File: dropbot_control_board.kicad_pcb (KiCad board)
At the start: 2 copper layers, 83.8 x 56.1 mm, 49 parts, among them J2 COMM_BUS, P3 POWER, P4 VOUT, P5 LIGHT, P6 MAGNET, P7 CONN_01X05, P8 CONN_01X03, Q1 IRF644PBF, Q2 TIP120, Q3 2N7002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

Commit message: Rename dropbot-control-board
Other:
- board text added: "DropBot control board v0.1"
- board text removed: "HV signal generator board v0.3"
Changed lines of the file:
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@@
   (page USLetter)
   (title_block
-    (title "HV signal generator board")
-    (date 2016-04-16)
-    (rev 0.3)
-    (company "Ryan Fobel")
+    (title "DropBot control board")
+    (date 2016-09-20)
+    (rev 0.1)
+    (company Sci-bots)
   )
   (layers
@@
     )
   )
-  (gr_text "HV signal generator board v0.3" (at 18.161 70.231) (layer F.SilkS)
+  (gr_text "DropBot control board v0.1" (at 18.161 70.231) (layer F.SilkS)
     (effects (font (size 1 1) (thickness 0.2)) (justify left))
   )

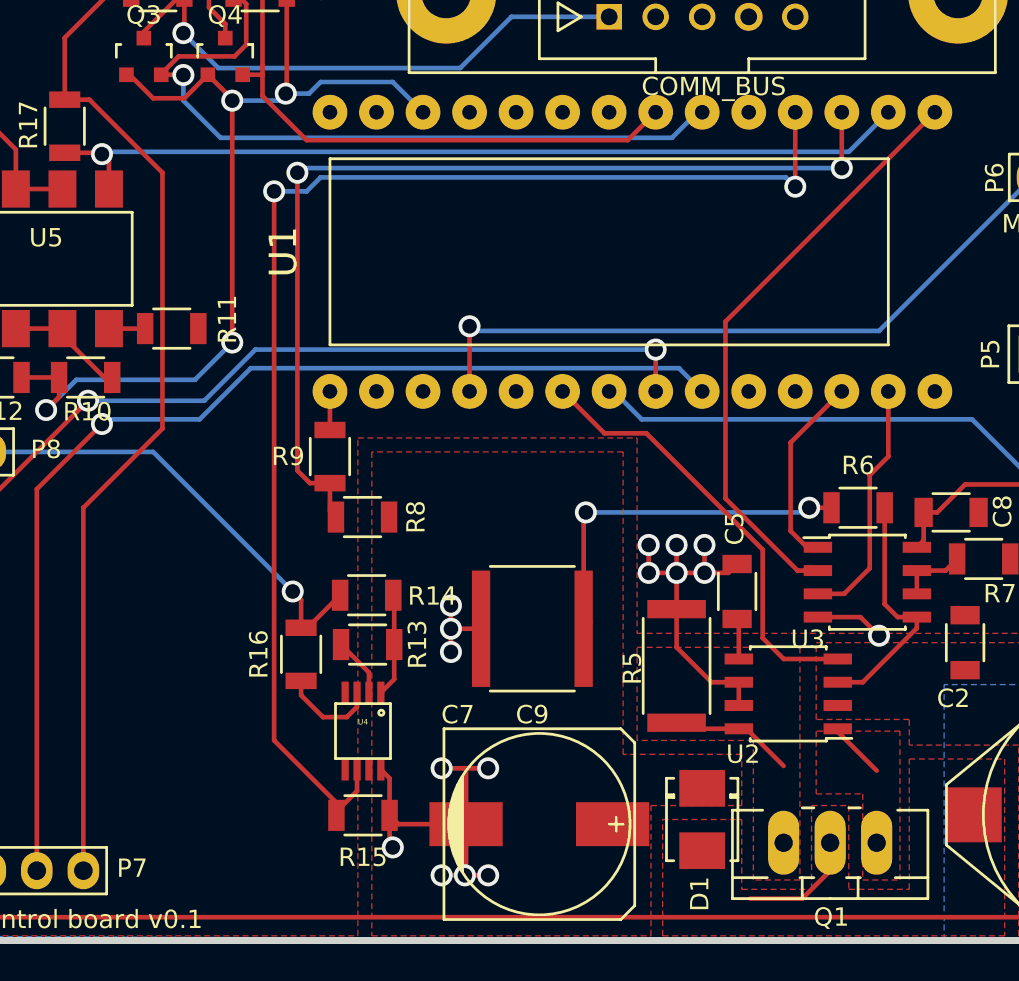
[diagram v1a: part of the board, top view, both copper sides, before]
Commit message: Fix routing of D3/OUTPUT_SELECT and add MAX1771...
Fix routing of D3/OUTPUT_SELECT and add MAX1771 current sensing.
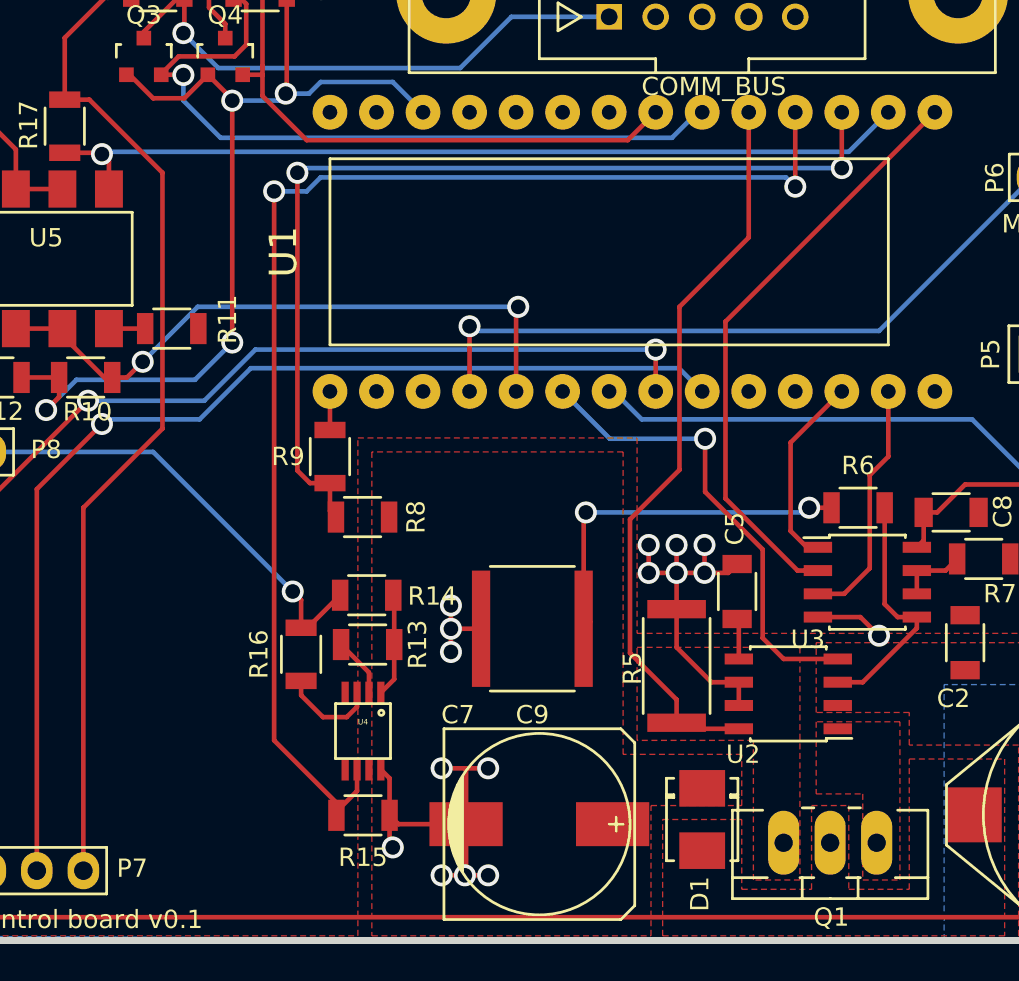
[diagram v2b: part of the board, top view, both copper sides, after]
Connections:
- net A2/CURRENT_SENSE renamed A2/HV507_CS
- Q1 pad 3: Net-(Q1-Pad3) -> A3/MAX1771_CS
- R10 pad 2: A3/OUTPUT_SELECT -> D3/OUTPUT_SELECT
- R5 pad 1: Net-(Q1-Pad3) -> A3/MAX1771_CS
- U1 pad 17: Net-(U1-Pad17) -> A3/MAX1771_CS
- U1 pad 3: Net-(U1-Pad3) -> D3/OUTPUT_SELECT
- U2 pad 8: Net-(Q1-Pad3) -> A3/MAX1771_CS
- U5 pad 2: A3/OUTPUT_SELECT -> D3/OUTPUT_SELECT
- U5 pad 3: A3/OUTPUT_SELECT -> D3/OUTPUT_SELECT
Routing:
- net A3/MAX1771_CS: track 0.00 -> 41.2 mm
- net D3/OUTPUT_SELECT: track 0.00 -> 35.4 mm, vias 0 -> 2
- net A3/OUTPUT_SELECT: track 7.02 -> 0.00 mm
- net Net-(Q1-Pad3): track 7.00 -> 0.00 mm
- net Net-(D1-Pad2): track 8.49 -> 3.49 mm
- net Net-(Q1-Pad1): track 3.51 -> 0.70 mm
- net D4/SHDN: track 23.9 -> 25.6 mm, vias 0 -> 1
- added copper zone on F.Cu, net A3/MAX1771_CS
- removed copper zone on F.Cu, net Net-(Q1-Pad3)

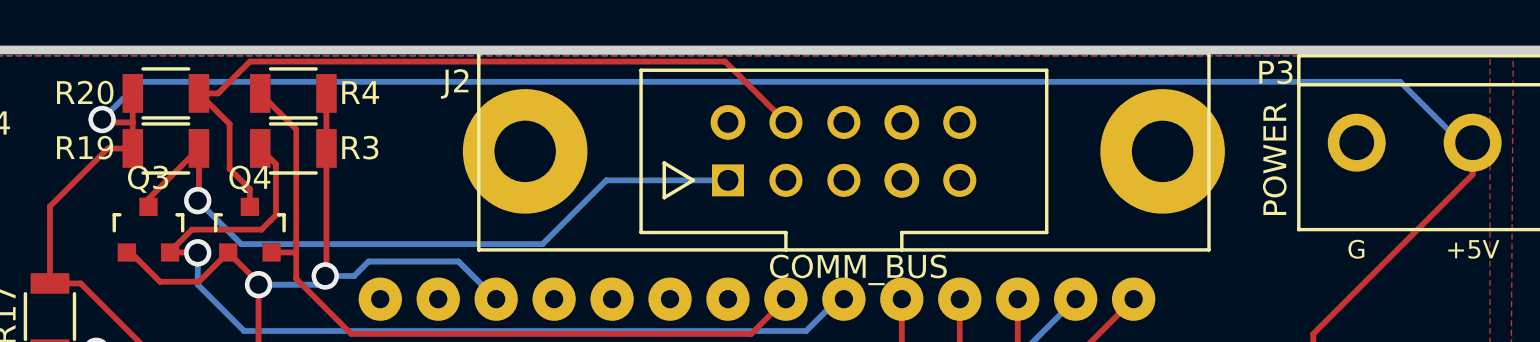
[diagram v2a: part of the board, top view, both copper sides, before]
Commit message: Connect 5V pin on COMM_BUS
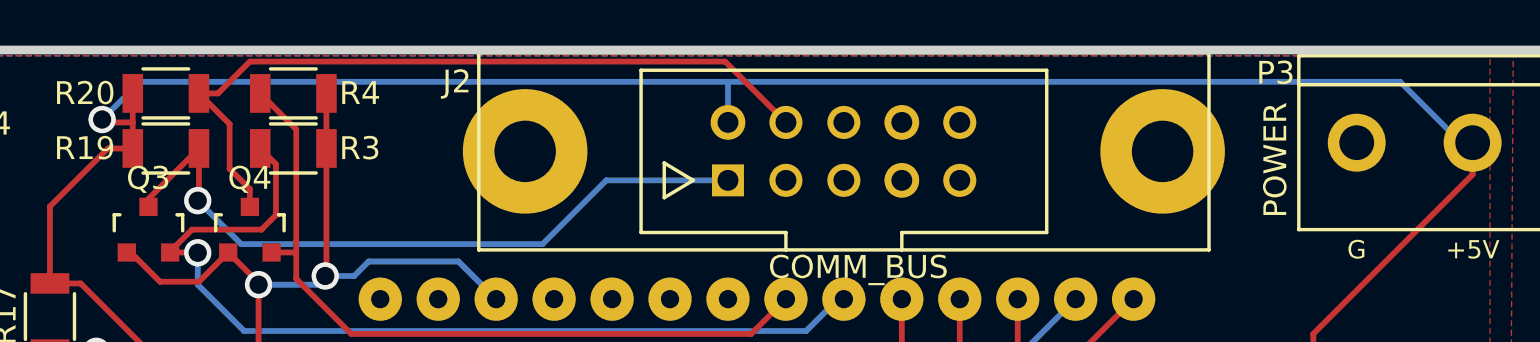
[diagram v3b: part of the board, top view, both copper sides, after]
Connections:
- J2 pad 2: Net-(J2-Pad2) -> +5V
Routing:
- net +5V: track 171.6 -> 173.4 mm

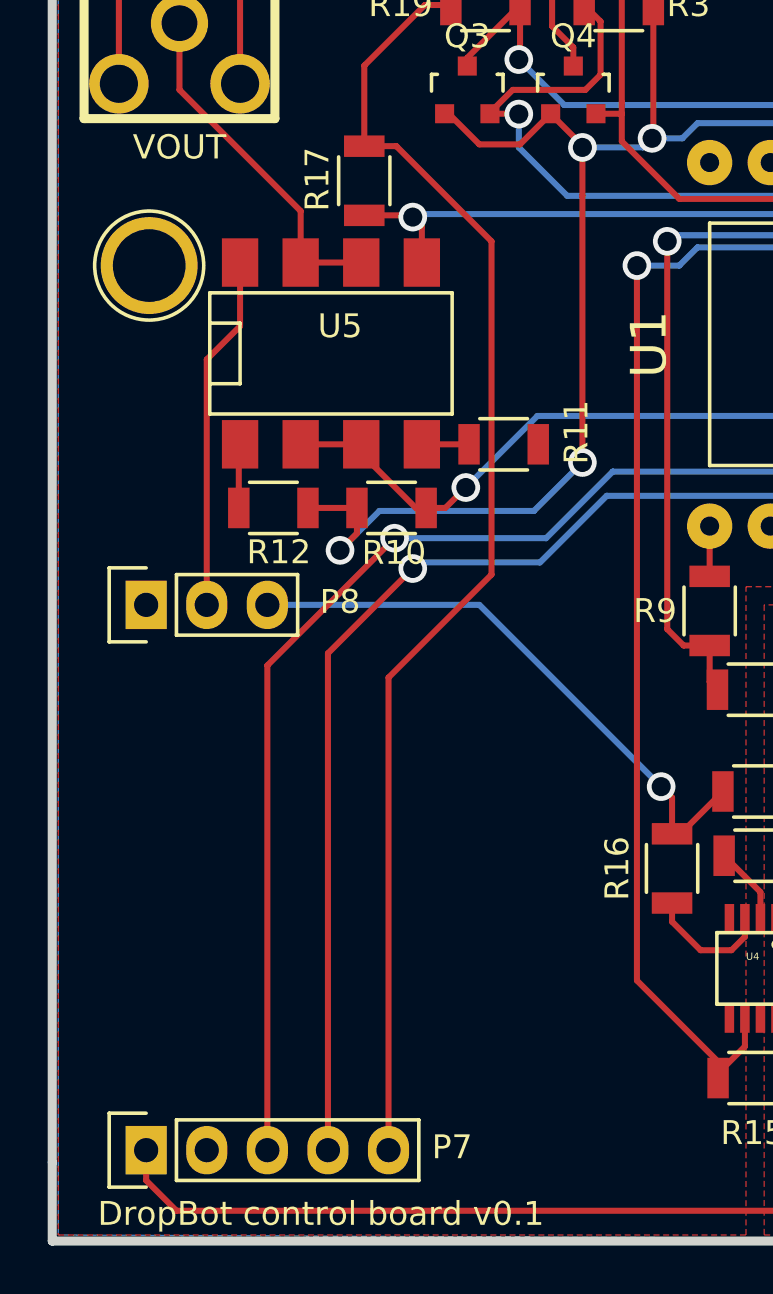
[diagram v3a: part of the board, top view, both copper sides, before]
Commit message: [WIP] Integrate HV square-wave driver (not routed)
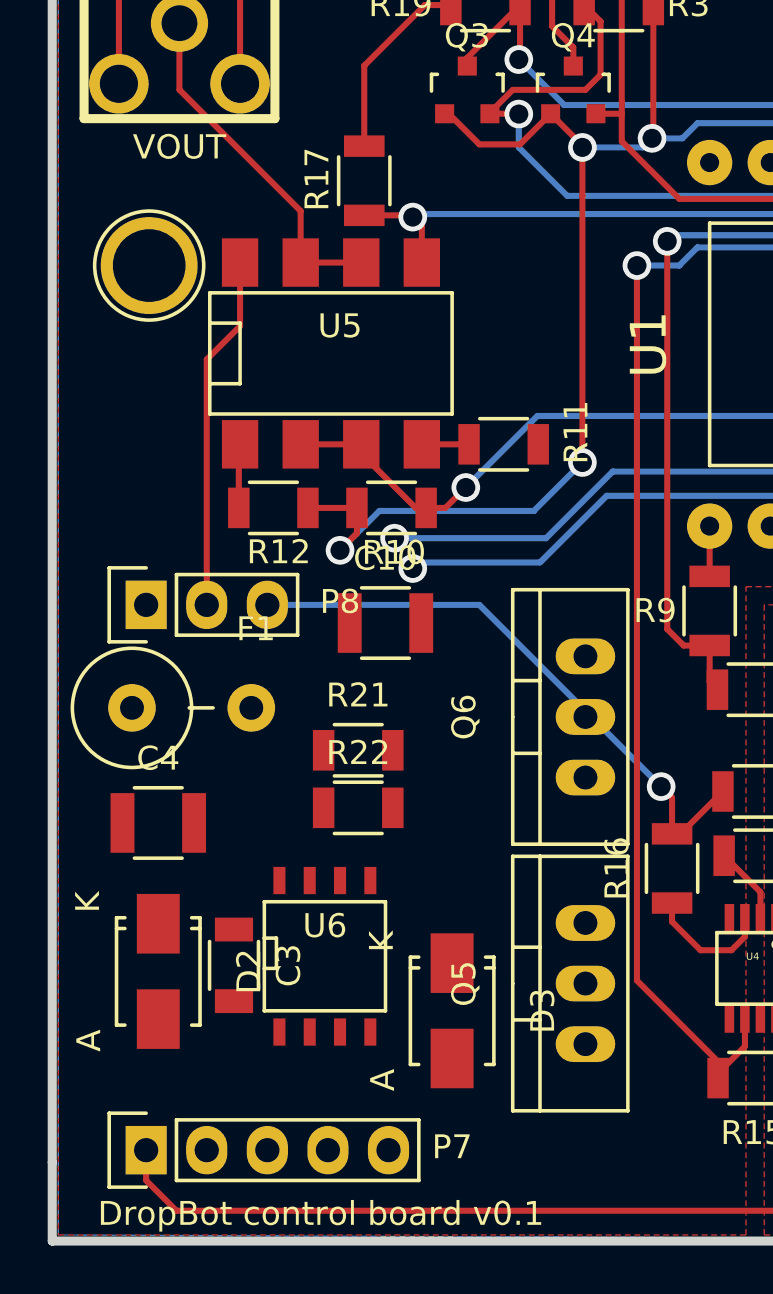
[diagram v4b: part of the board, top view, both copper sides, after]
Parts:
- added C10: C, Capacitors_SMD:C_1210, F.Cu at (30.2, 45.5)
- added C3: 0.1uF, Capacitors_SMD:C_1206, F.Cu at (23.9, 59.8)
- added C4: 0.1uF, Capacitors_SMD:C_1210, F.Cu at (20.7, 53.8)
- added D2: D, Diodes_SMD:SMA_Standard, F.Cu at (20.7, 60.1)
- added D3: D, Diodes_SMD:SMA_Standard, F.Cu at (33.0, 61.7)
- added F1: FUSE, Resistors_ThroughHole:Resistor_Vertical_RM5mm, F.Cu at (22.1, 49.0)
- added Q5: Q_NMOS_GDS, TO_SOT_Packages_THT:TO-220_Neutral123_Vertical, F.Cu at (38.6, 60.6)
- added Q6: Q_NMOS_GDS, TO_SOT_Packages_THT:TO-220_Neutral123_Vertical, F.Cu at (38.6, 49.4)
- added R21: 10, Resistors_SMD:R_1206, F.Cu at (29.1, 50.8)
- added R22: R, Resistors_SMD:R_1206, F.Cu at (29.1, 53.2)
- added U6: NCP5304, SMD_Packages:SOIC-8-N, F.Cu at (27.7, 59.4)
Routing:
- net +5V: track 173.4 -> 126.5 mm
- net D6/DRIVER_HI: track 62.3 -> 34.4 mm
- net D7/DRIVER_LO: track 60.7 -> 34.8 mm

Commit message: Re-do layout
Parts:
- added C11: 1uF, Capacitors_SMD:C_0805, F.Cu at (57.3, 45.0)
- added C12: 1pF, Capacitors_SMD:C_0805, F.Cu at (34.0, 50.0)
- added C13: 10pF, Capacitors_SMD:C_0805, F.Cu at (38.9, 49.9)
- added C14: 100pF, Capacitors_SMD:C_0805, F.Cu at (44.2, 49.9)
- added C15: 1nF, Capacitors_SMD:C_0805, F.Cu at (48.0, 49.9)
- added C16: 0.1uF, Capacitors_SMD:C_0805, F.Cu at (71.6, 44.1)
- added C17: 0.1uF, Capacitors_SMD:C_0805, F.Cu at (71.8, 38.0)
- added C18: 0.1uF, Capacitors_SMD:C_0805, F.Cu at (75.3, 38.2)
- added C19: 4.7nF, Capacitors_SMD:C_0805, F.Cu at (63.1, 46.7)
- added C20: 1nF, Capacitors_SMD:C_0805, F.Cu at (62.5, 35.2)
- added C21: 0.15uF, Capacitors_SMD:C_0805, F.Cu at (60.8, 37.5)
- added C22: 1nF, Capacitors_SMD:C_0805, F.Cu at (65.8, 47.6)
- added G***: LOGO, LOGO, F.Cu at (49.4, 89.2)
- added G***: LOGO, LOGO, F.Cu at (50.9, 83.2)
- added G***: LOGO, LOGO, F.Cu at (96.6, 50.4)
- added IC1: MCP6024, SMD_Packages:SOIC-14_N, F.Cu at (66.5, 40.5)
- added P1: FEEDBACK, footprints:JACK_SMA, F.Cu at (40.5, 28.2)
- added R23: 1Meg, Resistors_SMD:R_0805, F.Cu at (55.9, 42.4)
- added R24: 200, Resistors_SMD:R_0805, F.Cu at (33.8, 37.6)
- added R25: 10k, Resistors_SMD:R_0805, F.Cu at (72.8, 40.9)
- added R26: 2.2k, Resistors_SMD:R_0805, F.Cu at (73.5, 38.2)
- added R27: 1Meg, Resistors_SMD:R_0805, F.Cu at (73.5, 43.9)
- added R28: 200, Resistors_SMD:R_0805, F.Cu at (39.6, 37.6)
- added R29: 200, Resistors_SMD:R_0805, F.Cu at (45.0, 37.6)
- added R30: 200, Resistors_SMD:R_0805, F.Cu at (49.8, 37.6)
- added R31: 1.91k, Resistors_SMD:R_0805, F.Cu at (60.8, 39.2)
- added R32: 16.9k, Resistors_SMD:R_0805, F.Cu at (61.3, 44.7)
- added R33: 806, Resistors_SMD:R_0805, F.Cu at (60.8, 42.0)
- added R34: 13.3k, Resistors_SMD:R_0805, F.Cu at (60.3, 47.1)
- added U7: AQW216, SMD_Packages:DIP-8_SMD, F.Cu at (37.2, 43.7)
- added U8: AQW216, SMD_Packages:DIP-8_SMD, F.Cu at (47.9, 43.7)
- C2, C3, C5, C8: footprint Capacitors_SMD:C_1206 -> Capacitors_SMD:C_0805
- P7: value CONN_01X05 -> CONN_01X04; footprint Pin_Headers:Pin_Header_Straight_1x05 -> Pin_Headers:Pin_Header_Straight_1x04
- Q1, Q2: footprint TO_SOT_Packages_THT:TO-220_Neutral123_Vertical_LargePads -> TO_SOT_Packages_THT:TO-220_Neutral123_Horizontal_LargePads; moved to B.Cu
- Q5, Q6: footprint TO_SOT_Packages_THT:TO-220_Neutral123_Vertical -> TO_SOT_Packages_THT:TO-220_Neutral123_Horizontal_LargePads; moved to B.Cu
- R1, R10, R11, R12, R13, R14, R15, R16, R17, R18, R19, R2, R20, R21, R22, R3, R4, R7, R9: footprint Resistors_SMD:R_1206 -> Resistors_SMD:R_0805
- U1: value Teensy_3.1 -> Teensy_3.2; footprint footprints:Teensy-3.1 -> footprints:Teensy-3.2
- moved Q3 53.2 mm to (81.5, 46.2)
- moved R19 53.2 mm to (82.3, 42.7)
- moved R20 53.2 mm to (82.3, 40.3)
- moved Q4 53.2 mm to (86.0, 46.2)
- moved R3 53.2 mm to (87.9, 42.7)
- moved R4 53.2 mm to (87.9, 40.3)
- moved R14 35.1 mm to (69.6, 78.4)
- moved C3 33.6 mm to (39.8, 89.4), turned to 180 degrees
- moved R6 32.0 mm to (73.7, 79.8), turned to 90 degrees
- moved R9 31.6 mm to (61.6, 71.1)
- moved R8 31.2 mm to (63.6, 73.7)
- moved R13 30.8 mm to (68.3, 76.3)
- moved R17 29.9 mm to (37.1, 55.8), turned to 90 degrees
- moved C5 29.8 mm to (79.9, 78.7)
- moved C10 29.4 mm to (40.8, 72.9), turned to 90 degrees
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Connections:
- C3 pad 2: +5V -> +3.3V
- D2 pad 2: +5V -> +3.3V
- F1 pad 2: VOUT -> HVAC
- P4 pad 1: Net-(P4-Pad1) -> VOUT
- P6 pad 3: D2/SERVO -> D9/SERVO
- P7 pad 1: +12V -> GND
- P7 pad 2: GND -> D6/DRIVER_HI
- P7 pad 3: D6/DRIVER_HI -> D7/DRIVER_LO
- P7 pad 4: D7/DRIVER_LO -> +3.3V
- R10 pad 2: D3/OUTPUT_SELECT -> D8/OUTPUT_SELECT
- R17 pad 1: +5V -> +3.3V
- U1 pad 0: Net-(U1-Pad0) -> D0
- U1 pad 1: Net-(U1-Pad1) -> D1
- U1 pad 2: D2/SERVO -> D2
- U1 pad 3: D3/OUTPUT_SELECT -> D3
- U1 pad 8: Net-(U1-Pad8) -> D8/OUTPUT_SELECT
- U1 pad 9: Net-(U1-Pad9) -> D9/SERVO
- U5 pad 2: D3/OUTPUT_SELECT -> D8/OUTPUT_SELECT
- U5 pad 3: D3/OUTPUT_SELECT -> D8/OUTPUT_SELECT
- U5 pad 6: Net-(P4-Pad1) -> VOUT
- U5 pad 7: Net-(P4-Pad1) -> VOUT
- U5 pad 8: VOUT -> HVAC
- U6 pad 3: +5V -> +3.3V
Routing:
- net GND: track 84.1 -> 210.8 mm, vias 17 -> 27
- net +12V: track 123.1 -> 7.32 mm, vias 1 -> 0
- net +3.3V: track 56.1 -> 143.3 mm, vias 4 -> 3
- net VOUT: track 15.0 -> 81.7 mm, vias 0 -> 1
- net CUR_SENSE: track 0.00 -> 58.7 mm
- net D8/OUTPUT_SELECT: track 0.00 -> 51.7 mm, vias 0 -> 1
- net D1: track 0.00 -> 49.9 mm, vias 0 -> 2
- net D0: track 0.00 -> 49.0 mm, vias 0 -> 2
- net D6/DRIVER_HI: track 34.4 -> 78.1 mm
- net D2: track 0.00 -> 43.6 mm, vias 0 -> 2
- net D3: track 0.00 -> 42.7 mm, vias 0 -> 2
- net D2/SERVO: track 37.9 -> 0.00 mm, vias 1 -> 0
- net D3/OUTPUT_SELECT: track 35.4 -> 0.00 mm, vias 2 -> 0
- net +0.6V: track 0.00 -> 34.3 mm, vias 0 -> 2
- net HV: track 25.0 -> 58.8 mm, vias 1 -> 2
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- added copper zone on B.Cu, net HV
- added copper zone on B.Cu, net Net-(C10-Pad1)
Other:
- board size 83.8 x 56.1 mm -> 83.6 x 69.2 mm
- net class PWR added: clearance 0.127, trace_width 0.5, via_dia 1.2, via_drill 0.8
- board text added: "DropBot control board v0.1 2016"
- board text added: "Licensed under a Creative Commons Attribution-ShareAlike 3.0 Unported License."
- board text added: "http://sci-bots.com"
- board text removed: "+12V"
- board text removed: "+5V"
- board text removed: "DropBot control board v0.1"
